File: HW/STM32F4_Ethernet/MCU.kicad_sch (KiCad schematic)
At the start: 0 parts

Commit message: Progress backup
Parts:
- added C? (x14): 100nF, symbol Device:C_Small
- added C?: 100nF, Capacitor_SMD:C_0603_1608Metric_Pad1.08x0.95mm_HandSolder, symbol Device:C_Small
- added C? (x4): 2.2uF, symbol Device:C_Small
- added C? (x4): 12pF, Capacitor_SMD:C_0603_1608Metric_Pad1.08x0.95mm_HandSolder, symbol Device:C
- added C?: 4.7uF, symbol Device:C_Small
- added D?: 1N4148W, Diode_SMD:D_SOD-123, symbol Diode:1N4148W
- added D?: LED, LED_SMD:LED_0603_1608Metric_Pad1.05x0.95mm_HandSolder, symbol Device:LED
- added FB?: MPZ1608S601A, BEADC1608X95N, symbol MPZ1608S601A:MPZ1608S601A
- added H? (x4): (no value), MountingHole:MountingHole_3.2mm_M3_ISO7380_Pad, symbol Mechanical:MountingHole_Pad
- added JP?: Closed, symbol Jumper:Jumper_2_Bridged
- added R? (x2): 0, symbol Device:R
- added R? (x2): 100K, Resistor_SMD:R_0603_1608Metric_Pad0.98x0.95mm_HandSolder, symbol Device:R_Small
- added R?: 470, Resistor_SMD:R_0603_1608Metric_Pad0.98x0.95mm_HandSolder, symbol Device:R_Small
- added R?: 10K, symbol Device:R
- added SW? (x3): SW_Push, Button_Switch_SMD:SW_SPST_B3U-1000P-B, symbol Switch:SW_Push
- added U?: STM32F407ZGTx, Package_QFP:LQFP-144_20x20mm_P0.5mm, symbol MCU_ST_STM32F4:STM32F407ZGTx
- added Y?: 25Mhz, Crystal:Crystal_SMD_3225-4Pin_3.2x2.5mm_HandSoldering, symbol Device:Crystal_GND24
- added Y?: 32.768KHz, Crystal:Crystal_SMD_3225-4Pin_3.2x2.5mm_HandSoldering, symbol Device:Crystal_GND24
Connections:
- new net: D?.2 (A), R?.2
- new net: C?.2, U?.71 (VCAP_1)
- new net: C?.2, U?.106 (VCAP_2)
- new net +3V3: C?.1, C?.1, C?.1, C?.1, C?.1, C?.1, C?.1, C?.1, C?.1, C?.1, C?.1, C?.1, C?.1, C?.1, C?.1, C?.1, D?.1 (K), FB?.1, R?.1, R?.1, R?.1, SW?.2, SW?.2, U?.108 (VDD), U?.121 (VDD), U?.131 (VDD), U?.144 (VDD), U?.17 (VDD), U?.30 (VDD), U?.39 (VDD), U?.52 (VDD), U?.62 (VDD), U?.72 (VDD), U?.84 (VDD), U?.95 (VDD)
- new net B0: R?.1, SW?.1, U?.34 (PA0)
- new net BOOT0: R?.1, SW?.1, U?.138 (BOOT0)
- new net GND: C?.1, C?.1, C?.2, C?.2, C?.2, C?.2, C?.2, C?.2, C?.2, C?.2, C?.2, C?.2, C?.2, C?.2, C?.2, C?.2, C?.2, C?.2, C?.2, C?.2, C?.2, C?.2, C?.2, H?.1, H?.1, H?.1, H?.1, JP?.1 (A), R?.2, R?.2, R?.2, SW?.2, U?.107 (VSS), U?.120 (VSS), U?.130 (VSS), U?.16 (VSS), U?.38 (VSS), U?.51 (VSS), U?.61 (VSS), U?.83 (VSS), U?.94 (VSS), Y?.2, Y?.2, Y?.4, Y?.4
- new net HSE+: C?.1, U?.23 (PH0), Y?.1
- new net HSE-: C?.1, U?.24 (PH1), Y?.3
- new net LD1: D?.1 (K), U?.7 (PC13)
- new net LSE+: C?.1, U?.8 (PC14), Y?.1
- new net LSE-: C?.1, U?.9 (PC15), Y?.3
- new net PDR_ON: R?.1, R?.2, U?.143 (PDR_ON)
- new net STM32_VDDA: C?.1, FB?.2, U?.33 (VDDA)
- new net STM32_VSSA: C?.2, JP?.2 (B), U?.31 (VSSA)
- new net USB_D+: U?.104 (PA12)
- new net USB_D-: U?.103 (PA11)
- new net ~{RESET}: C?.1, D?.2 (A), R?.2, SW?.1, U?.25 (NRST)
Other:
- note added: "(X7R Low ESR)"
- note added: "17, 30, 39, 52, 62, 72, 84, 95, 108, 121, 131, 144"
- note added: "BOOT0"
- note added: "BUTTON"
- note added: "DNI"
- note added: "LED"
- note added: "Two 0 Ω resistors connected to: - VSS for the STM32F10xx - VSS, VDD or NC for the STM32F2xx - VDD or signal from external power supply supervisor for the STM32F4xx"

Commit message: Progress backup. add SRAM
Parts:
- added U1: K6F8016U6B, symbol K6F8016U6B:K6F8016U6B
- gave numbers to parts that had none: 44
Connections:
- net +3V3: now also U1.D6 (VCC[2]), U1.E1 (VCC[2])
- net GND: now also U1.D1 (VSS[3]), U1.E3 (VSS[3]), U1.E6 (VSS[3])

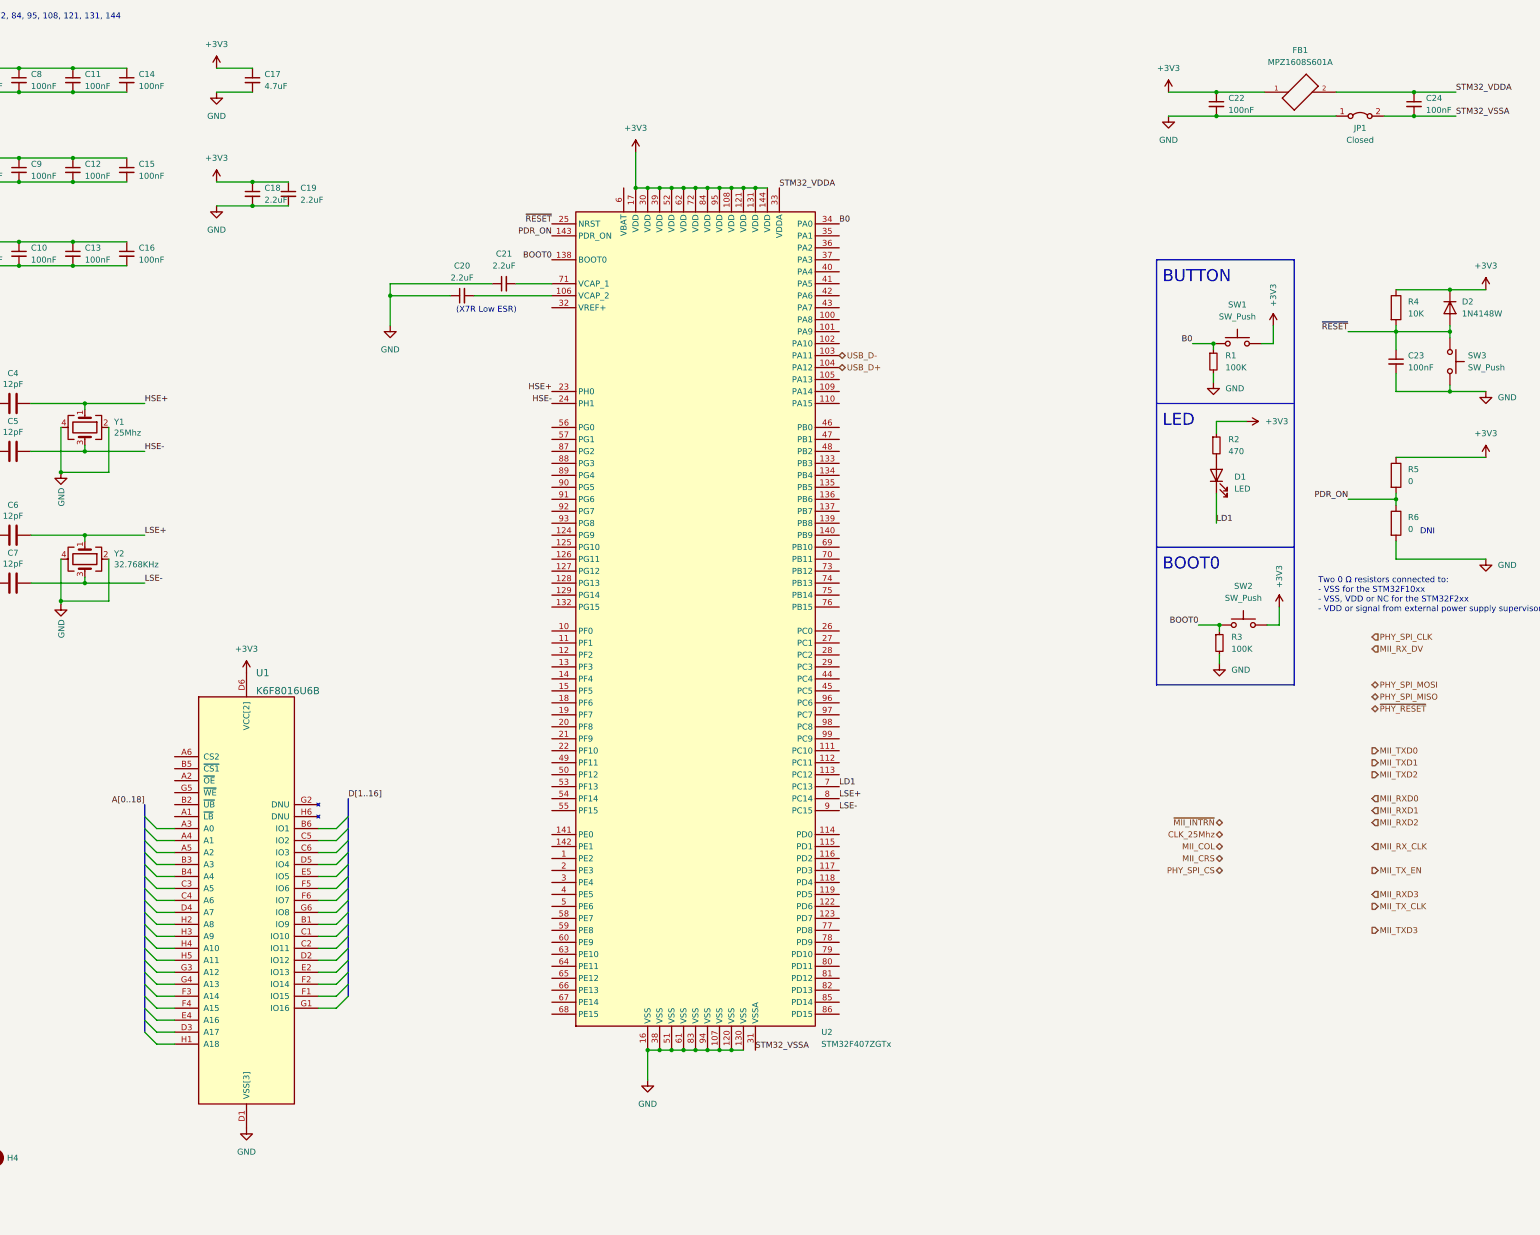
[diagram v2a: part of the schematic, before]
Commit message: Sample PCB. Need to update RLC Size
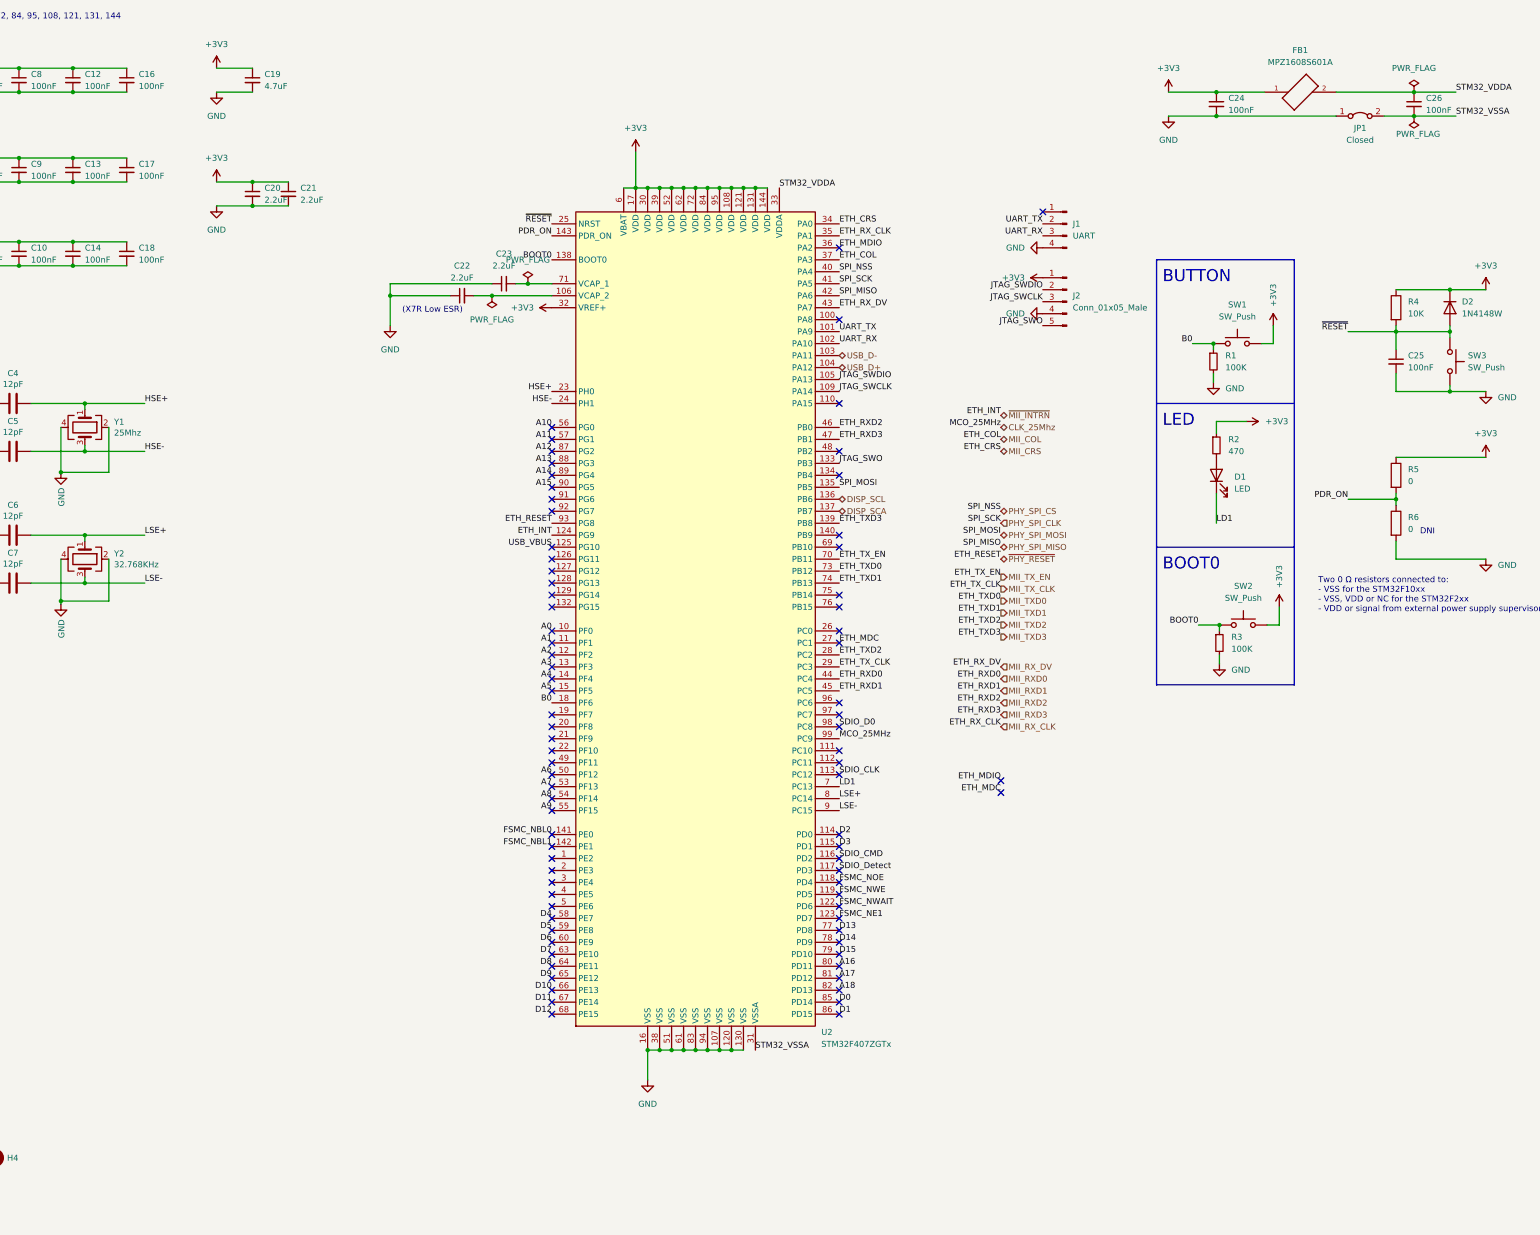
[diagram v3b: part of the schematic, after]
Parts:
- removed U1: K6F8016U6B, symbol K6F8016U6B:K6F8016U6B
- added J1: UART, Connector_PinHeader_2.54mm:PinHeader_1x04_P2.54mm_Vertical, symbol Connector:Conn_01x04_Male
- added J2: Conn_01x05_Male, Connector_PinHeader_2.54mm:PinHeader_1x05_P2.54mm_Vertical, symbol Connector:Conn_01x05_Male
- C1, C10, C2, C3, C8, C9: footprint (none) -> Capacitor_SMD:C_0603_1608Metric_Pad1.08x0.95mm_HandSolder
- C12: renamed from C11; footprint (none) -> Capacitor_SMD:C_0603_1608Metric_Pad1.08x0.95mm_HandSolder
- C13: renamed from C12; footprint (none) -> Capacitor_SMD:C_0603_1608Metric_Pad1.08x0.95mm_HandSolder
- C14: renamed from C13; footprint (none) -> Capacitor_SMD:C_0603_1608Metric_Pad1.08x0.95mm_HandSolder
- C16: renamed from C14; footprint (none) -> Capacitor_SMD:C_0603_1608Metric_Pad1.08x0.95mm_HandSolder
- C17: renamed from C15; footprint (none) -> Capacitor_SMD:C_0603_1608Metric_Pad1.08x0.95mm_HandSolder
- C18: renamed from C16; footprint (none) -> Capacitor_SMD:C_0603_1608Metric_Pad1.08x0.95mm_HandSolder
- C19: renamed from C17; footprint (none) -> Capacitor_SMD:C_0805_2012Metric_Pad1.18x1.45mm_HandSolder
- C20: renamed from C18; footprint (none) -> Capacitor_SMD:C_0805_2012Metric_Pad1.18x1.45mm_HandSolder
- C21: renamed from C19; footprint (none) -> Capacitor_SMD:C_0805_2012Metric_Pad1.18x1.45mm_HandSolder
- C22: renamed from C20; footprint (none) -> Capacitor_SMD:C_0805_2012Metric_Pad1.18x1.45mm_HandSolder
- C23: renamed from C21; footprint (none) -> Capacitor_SMD:C_0805_2012Metric_Pad1.18x1.45mm_HandSolder
- C24: renamed from C22; footprint (none) -> Capacitor_SMD:C_0603_1608Metric_Pad1.08x0.95mm_HandSolder
- C26: renamed from C24; footprint (none) -> Capacitor_SMD:C_0603_1608Metric_Pad1.08x0.95mm_HandSolder
- FB1: footprint BEADC1608X95N -> MPZ1608S601A:BEADC1608X95N
- JP1: footprint (none) -> Jumper:SolderJumper-2_P1.3mm_Open_TrianglePad1.0x1.5mm
- R4, R5, R6: footprint (none) -> Resistor_SMD:R_0603_1608Metric_Pad0.98x0.95mm_HandSolder
- renumbered C23 to C25
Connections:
- net +3V3: now also U2.32 (VREF+), U2.6 (VBAT), J2.1 (Pin_1)
- net B0: now also U2.18 (PF6); no longer U2.34 (PA0)
- net CLK_25Mhz: now also U2.99 (PC9)
- net GND: now also J1.4 (Pin_4), J2.4 (Pin_4)
- net MII_COL: now also U2.37 (PA3)
- net MII_CRS: now also U2.34 (PA0)
- net MII_RXD0: now also U2.44 (PC4)
- net MII_RXD1: now also U2.45 (PC5)
- net MII_RXD2: now also U2.46 (PB0)
- net MII_RXD3: now also U2.47 (PB1)
- net MII_RX_CLK: now also U2.35 (PA1)
- net MII_RX_DV: now also U2.43 (PA7)
- net MII_TXD0: now also U2.73 (PB12)
- net MII_TXD1: now also U2.74 (PB13)
- net MII_TXD2: now also U2.28 (PC2)
- net MII_TXD3: now also U2.139 (PB8)
- net MII_TX_CLK: now also U2.29 (PC3)
- net MII_TX_EN: now also U2.70 (PB11)
- net PHY_SPI_CLK: now also U2.41 (PA5)
- net PHY_SPI_CS: now also U2.40 (PA4)
- net PHY_SPI_MISO: now also U2.42 (PA6)
- net PHY_SPI_MOSI: now also U2.135 (PB5)
- net ~{MII_INTRN}: now also U2.124 (PG9)
- net ~{PHY_RESET}: now also U2.93 (PG8)
- net A0: now reaches U2.10 (PF0)
- net UART_TX: now reaches U2.101 (PA9)
- net UART_TX: now also J1.2 (Pin_2)
- net UART_RX: now reaches U2.102 (PA10)
- net UART_RX: now also J1.3 (Pin_3)
- net JTAG_SWDIO: now reaches U2.105 (PA13)
- net JTAG_SWDIO: now also J2.2 (Pin_2)
- net JTAG_SWCLK: now reaches U2.109 (PA14)
- net JTAG_SWCLK: now also J2.3 (Pin_3)
- net A1: now reaches U2.11 (PF1)
- net SDIO_CLK: now reaches U2.113 (PC12)
- net D2: now reaches U2.114 (PD0)
- net D3: now reaches U2.115 (PD1)
- net SDIO_CMD: now reaches U2.116 (PD2)
- net SDIO_Detect: now reaches U2.117 (PD3)
- net FSMC_NOE: now reaches U2.118 (PD4)
- net FSMC_NWE: now reaches U2.119 (PD5)
- net A2: now reaches U2.12 (PF2)
- net FSMC_NWAIT: now reaches U2.122 (PD6)
- net FSMC_NE1: now reaches U2.123 (PD7)
- net USB_VBUS: now reaches U2.125 (PG10)
- net A3: now reaches U2.13 (PF3)
- net JTAG_SWO: now reaches U2.133 (PB3)
- net JTAG_SWO: now also J2.5 (Pin_5)
- net DISP_SCL: now reaches U2.136 (PB6)
- net DISP_SCA: now reaches U2.137 (PB7)
- net A4: now reaches U2.14 (PF4)
- net FSMC_NBL0: now reaches U2.141 (PE0)
- net FSMC_NBL1: now reaches U2.142 (PE1)
- net A5: now reaches U2.15 (PF5)
- net ETH_MDC: now reaches U2.27 (PC1)
- net ETH_MDIO: now reaches U2.36 (PA2)
- net A6: now reaches U2.50 (PF12)
- net A7: now reaches U2.53 (PF13)
- net A8: now reaches U2.54 (PF14)
- net A9: now reaches U2.55 (PF15)
- net A10: now reaches U2.56 (PG0)
- net A11: now reaches U2.57 (PG1)
- net D4: now reaches U2.58 (PE7)
- net D5: now reaches U2.59 (PE8)
- net D6: now reaches U2.60 (PE9)
- net D7: now reaches U2.63 (PE10)
- net D8: now reaches U2.64 (PE11)
- net D9: now reaches U2.65 (PE12)
- net D10: now reaches U2.66 (PE13)
- net D11: now reaches U2.67 (PE14)
- net D12: now reaches U2.68 (PE15)
- net D13: now reaches U2.77 (PD8)
- net D14: now reaches U2.78 (PD9)
- net D15: now reaches U2.79 (PD10)
- net A16: now reaches U2.80 (PD11)
- net A17: now reaches U2.81 (PD12)
- net A18: now reaches U2.82 (PD13)
- net D0: now reaches U2.85 (PD14)
- net D1: now reaches U2.86 (PD15)
- net A12: now reaches U2.87 (PG2)
- net A13: now reaches U2.88 (PG3)
- net A14: now reaches U2.89 (PG4)
- net A15: now reaches U2.90 (PG5)
- net SDIO_D0: now reaches U2.98 (PC8)
- no-connect marks 0 -> 81
